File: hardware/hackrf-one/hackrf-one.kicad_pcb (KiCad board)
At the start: 4 copper layers, 120 x 75 mm, 435 parts, among them J10 GND_CLIP, J11 Connector_USB_C_Receptacle_US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, J2 RF-SHIELD-FRAME, J3 RF-SHIELD-COVER, J4 MOUNTING_HOLE, J5 MOUNTING_HOLE, J6 MOUNTING_HOLE, J7 MOUNTING_HOLE, J8 MOUNTING_HOLE, J9 MOUNTING_HOLE, P1 1V8, P13 GPO1, P14 XCVR_CLKOUT, P15 INTR, P16 CLKIN, P17 GPO6, P18 OEB, P19 GPO3, P2 CLKOUT, P20 GPIO, P21 REF_IN, P22 I2S, P23 DBGEN, P24 TRST, P25 LPC_ISP, P26 LPC_JTAG, P27 MIXER_SDATA, P28 SD, P29 CPLD_JTAG, P3 GND, P30 BANK2_AUX, P31 MIXER_SCLK, P32 MIXER_ENX, P33 MIXER_RESETX, P34 MIX_BYPASS, P35 !MIX_BYPASS, P36 VAA, P37 SCL, P38 SDA, P39 SSP1_SCK, P4 ANTENNA, P40 SSP1_MOSI, P41 SSP1_MISO, P43 RX, P44 HP, P45 LP, P46 TX_MIX_BP, P47 RX_MIX_BP, P48 TX_AMP, P49 RX_AMP, P5 LEDS, P50 AMP_BYPASS, P51 !TX_AMP_PWR, P52 !RX_AMP_PWR, P53 CS_XCVR, P54 CS_AD, P55 TXENABLE, P56 RXENABLE, P57 XTAL2, P58 GCK1, P59 GCK2, P6 GPO4, P60 SGPIO_CLK, P61 DA0, P62 DA7, P63 DD0, P64 DD9, P65 DA4, P66 DD5, P67 RSSI, P68 SPIFI_CS, P69 VREGMODE, P7 GPO2, P70 EN_1V8, P72 GP_CLKIN, P73 P1_2, P74 P1_1, P75 GP_CLKIN, P76 GP_CLKIN, P77 GP_CLKIN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

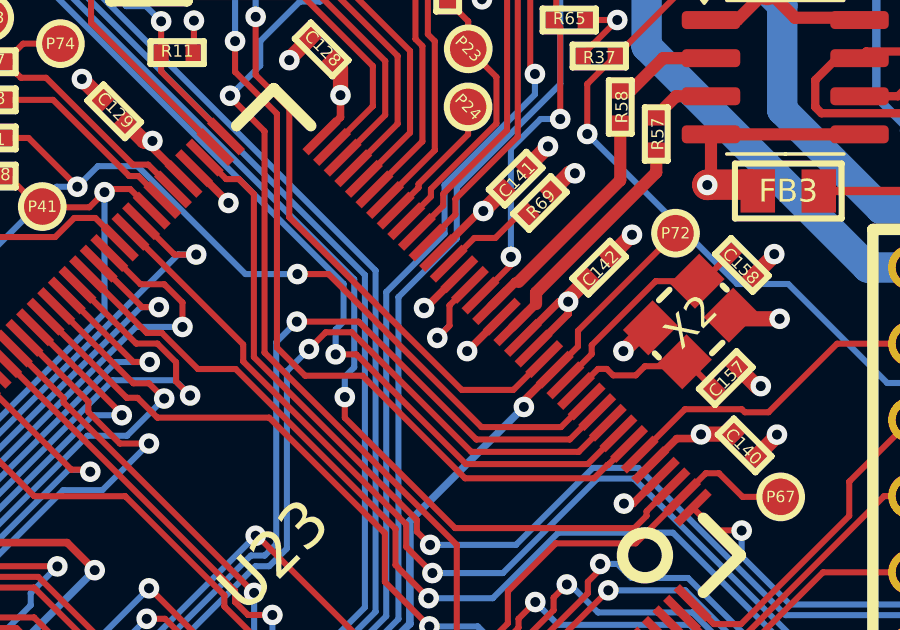
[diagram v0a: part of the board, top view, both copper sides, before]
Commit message: Leave ID pin open, to signal it's a USB device
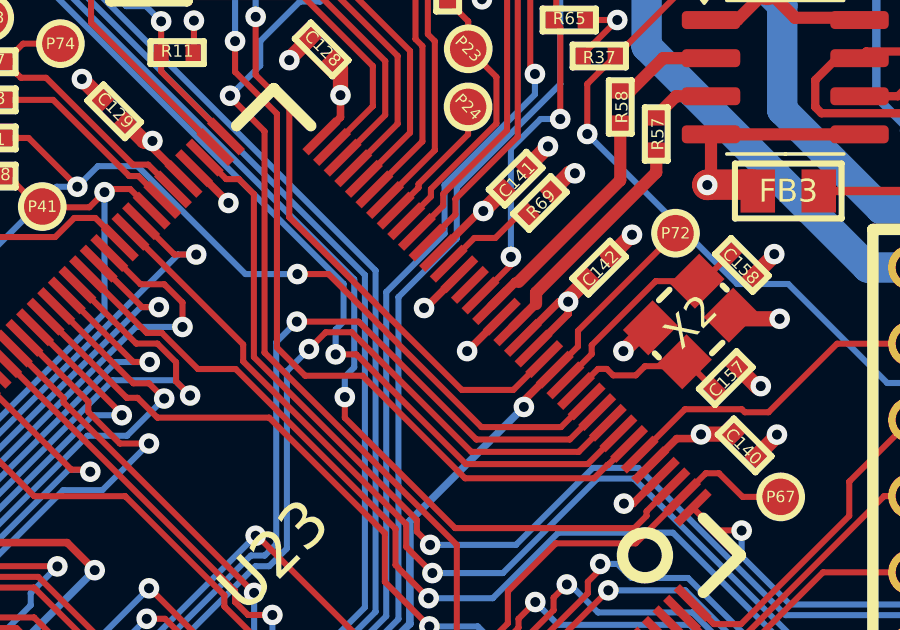
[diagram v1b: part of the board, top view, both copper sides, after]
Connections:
- U23 pad 22: GND -> unconnected-(U23-USB0_ID-Pad22)
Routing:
- net GND: track 599.4 -> 596.7 mm, vias 220 -> 219

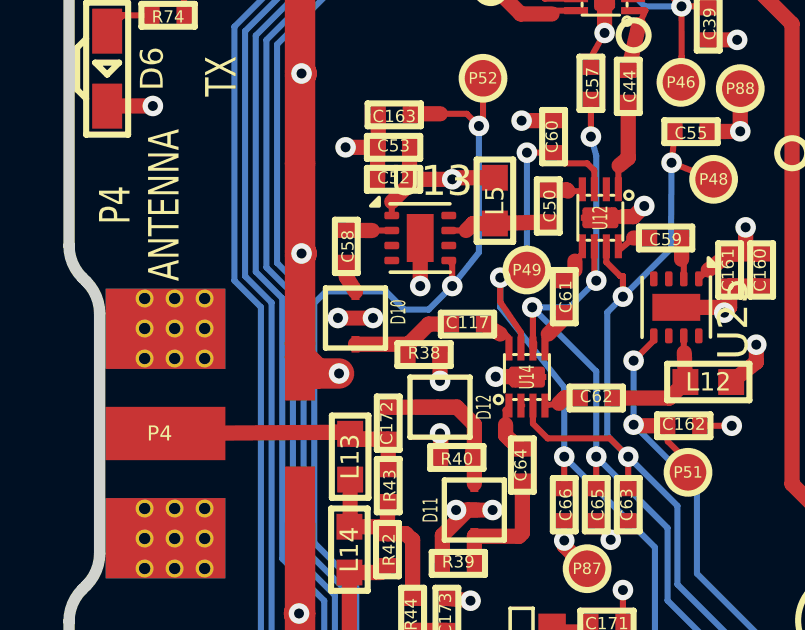
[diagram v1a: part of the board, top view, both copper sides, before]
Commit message: Changed from SMP1330 to CLA4611 to improve performance to 6GHz
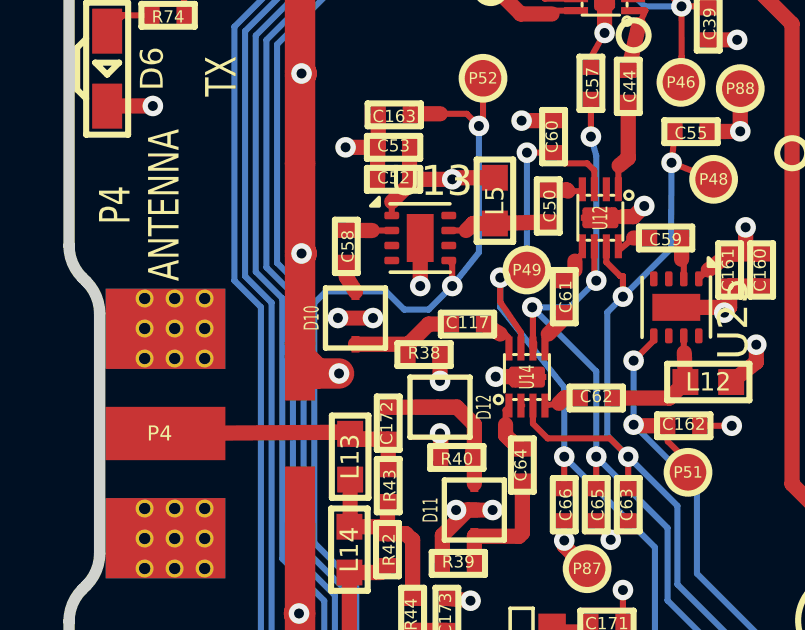
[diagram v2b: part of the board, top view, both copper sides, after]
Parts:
- D10, D11, D12: value SMP1330 -> CLA4611; footprint gsg-modules:SMP1330-085LF -> gsg-modules:SkyworksLimiterDiode
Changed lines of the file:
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@@
 		)
 	)
-	(footprint "gsg-modules:SMP1330-085LF"
+	(footprint "gsg-modules:SkyworksLimiterDiode"
 		(layer "F.Cu")
 		(at 58.3702 139.4058 -90)
 		(property "Reference" "D10"
-			(at -0.20066 -1.43002 90)
+			(at 0 1.4605 90)
 			(layer "F.SilkS")
 			(effects
@@
 			)
 		)
-		(property "Value" "SMP1330"
+		(property "Value" "CLA4611"
 			(at 0 -0.889 90)
 			(layer "F.Fab")
@@
 			)
 		)
-		(property "Footprint" "gsg-modules:SMP1330-085LF"
+		(property "Footprint" "gsg-modules:SkyworksLimiterDiode"
 			(at 0 0 -90)
 			(layer "F.Fab")
@@
 			)
 		)
-		(property "Part Number" "SMP1330-085LF"
-			(at 0 0 -90)
-			(unlocked yes)
-			(layer "F.Fab")
-			(hide yes)
-			(effects
-				(font
-					(size 1 1)
-					(thickness 0.15)
-				)
-			)
-		)
-		(property ki_fp_filters "TO-???* *_Diode_* *SingleDiode* D_*")
+		(property "Part Number" "CLA4611-085LF"
+			(at 0 0 -90)
+			(unlocked yes)
+			(layer "F.Fab")
+			(hide yes)
+			(effects
+				(font
+					(size 1 1)
+					(thickness 0.15)
+				)
+			)
+		)
+		(property ki_fp_filters "PIN_*")
 		(sheetname "frontend")
 		(sheetfile "frontend.kicad_sch")
@@
 		)
 	)
-	(footprint "gsg-modules:SMP1330-085LF"
+	(footprint "gsg-modules:SkyworksLimiterDiode"
 		(layer "F.Cu")
 		(at 62.3326 145.8066 -90)
@@
 			)
 		)
-		(property "Value" "SMP1330"
+		(property "Value" "CLA4611"
 			(at 0 -0.889 90)
 			(layer "F.Fab")
@@
 			)
 		)
-		(property "Footprint" "gsg-modules:SMP1330-085LF"
+		(property "Footprint" "gsg-modules:SkyworksLimiterDiode"
 			(at 0 0 -90)
 			(layer "F.Fab")
@@
 			)
 		)
-		(property "Part Number" "SMP1330-085LF"
-			(at 0 0 -90)
-			(unlocked yes)
-			(layer "F.Fab")
-			(hide yes)
-			(effects
-				(font
-					(size 1 1)
-					(thickness 0.15)
-				)
-			)
-		)
-		(property ki_fp_filters "TO-???* *_Diode_* *SingleDiode* D_*")
+		(property "Part Number" "CLA4611-085LF"
+			(at 0 0 -90)
+			(unlocked yes)
+			(layer "F.Fab")
+			(hide yes)
+			(effects
+				(font
+					(size 1 1)
+					(thickness 0.15)
+				)
+			)
+		)
+		(property ki_fp_filters "PIN_*")
 		(sheetname "frontend")
 		(sheetfile "frontend.kicad_sch")
@@
 		)
 	)
-	(footprint "gsg-modules:SMP1330-085LF"
+	(footprint "gsg-modules:SkyworksLimiterDiode"
 		(layer "F.Cu")
 		(at 61.1896 142.3776 90)
 		(property "Reference" "D12"
-			(at 0 1.4605 90)
+			(at 0 1.4605 -90)
 			(layer "F.SilkS")
 			(effects
@@
 			)
 		)
-		(property "Value" "SMP1330"
-			(at 0 -0.889 90)
+		(property "Value" "CLA4611"
+			(at 0 -0.889 -90)
 			(layer "F.Fab")
 			(effects
@@
 			)
 		)
-		(property "Footprint" "gsg-modules:SMP1330-085LF"
+		(property "Footprint" "gsg-modules:SkyworksLimiterDiode"
 			(at 0 0 90)
 			(layer "F.Fab")
@@
 			)
 		)
-		(property "Part Number" "SMP1330-085LF"
+		(property "Part Number" "CLA4611-085LF"
 			(at 0 0 90)
 			(unlocked yes)
@@
 			)
 		)
-		(property ki_fp_filters "TO-???* *_Diode_* *SingleDiode* D_*")
+		(property ki_fp_filters "PIN_*")
 		(sheetname "frontend")
 		(sheetfile "frontend.kicad_sch")

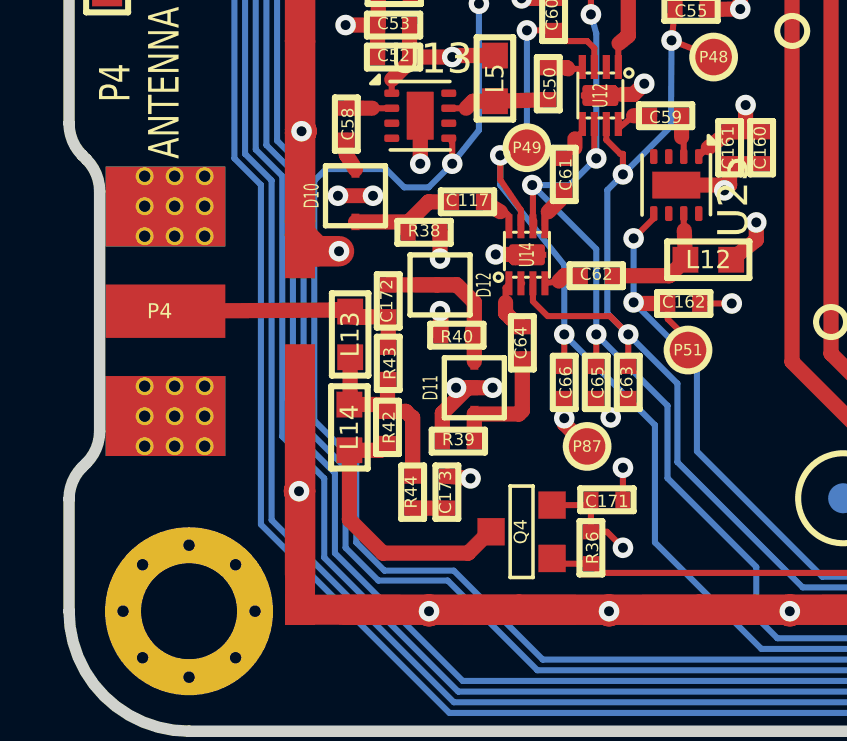
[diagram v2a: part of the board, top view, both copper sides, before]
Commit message: Changed limiter to CLA4611. Added Schottky bias tee diode
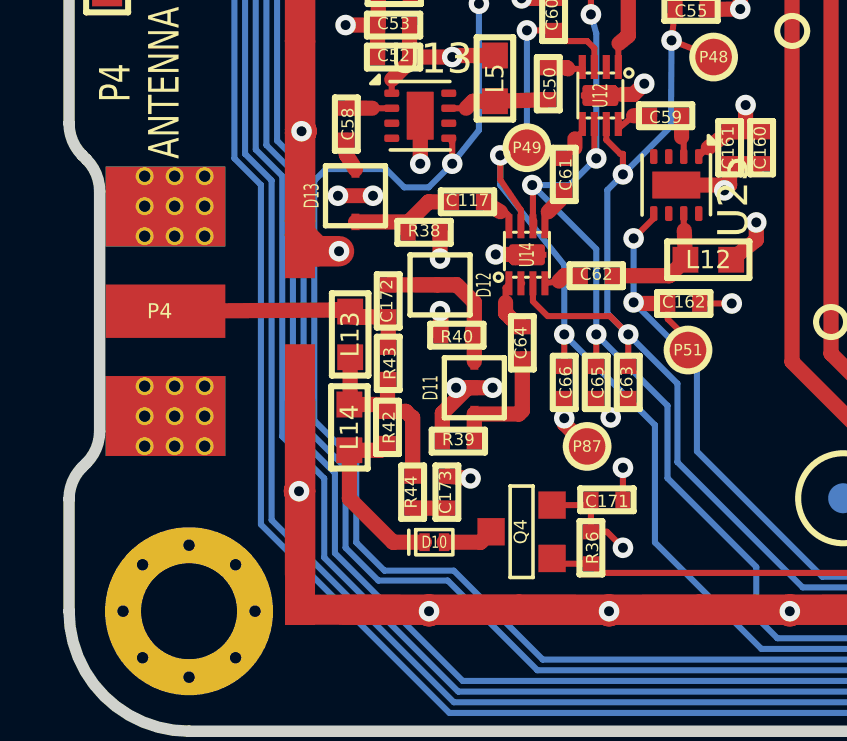
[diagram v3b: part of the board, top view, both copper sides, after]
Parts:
- added D10: D_Schottky, gsg-modules:DSN1006-2, F.Cu at (61.0, 151.0)
- renumbered D10 to D13
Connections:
- L14 pad 1: Net-(L14-Pad1) -> Net-(D10-K)
- Q4 pad D: Net-(L14-Pad1) -> Net-(D10-A)
- R42 pad 1: Net-(L14-Pad1) -> Net-(D10-K)
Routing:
- net Net-(L14-Pad1): track 9.16 -> 0.00 mm
- net Net-(D10-K): track 0.00 -> 6.08 mm
- net Net-(D10-A): track 0.00 -> 1.71 mm
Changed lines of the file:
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@@
 	(net 228 "/frontend/RX_AMP_IN")
 	(net 229 "Net-(C173-Pad2)")
-	(net 230 "Net-(L14-Pad1)")
+	(net 230 "Net-(D13-A2)")
 	(net 231 "Net-(U1-RFC)")
 	(net 232 "Net-(U2-RF1)")
@@
 	(net 269 "Net-(U10-RF1)")
 	(net 270 "Net-(U11-RF2)")
-	(net 271 "Net-(D10-A2)")
+	(net 271 "Net-(D10-K)")
 	(net 272 "Net-(U13-RFIN)")
 	(net 273 "Net-(U25-RFIN)")
@@
 	(net 389 "Net-(FB3-Pad1)")
 	(net 390 "unconnected-(U23-USB0_ID-Pad22)")
+	(net 391 "Net-(D10-A)")
 	(footprint "gsg-modules:LTST-S220"
 		(layer "F.Cu")
@@
 			(size 0.508 0.5588)
 			(layers "F.Cu" "F.Paste" "F.Mask")
-			(net 271 "Net-(D10-A2)")
+			(net 230 "Net-(D13-A2)")
 			(pintype "passive")
 			(die_length -2147.483637)
@@
 			(size 0.9144 0.9144)
 			(layers "F.Cu" "F.Paste" "F.Mask")
-			(net 230 "Net-(L14-Pad1)")
+			(net 391 "Net-(D10-A)")
 			(pinfunction "D")
 			(pintype "passive")
@@
 			(size 0.508 0.5588)
 			(layers "F.Cu" "F.Paste" "F.Mask")
-			(net 230 "Net-(L14-Pad1)")
+			(net 271 "Net-(D10-K)")
 			(pintype "passive")
 			(die_length -2147.483637)
@@
 			(size 0.8636 0.8636)
 			(layers "F.Cu" "F.Paste" "F.Mask")
-			(net 230 "Net-(L14-Pad1)")
+			(net 271 "Net-(D10-K)")
 			(pinfunction "1")
 			(pintype "passive")
@@
 		(layer "F.Cu")
 		(at 58.3702 139.4058 -90)
-		(property "Reference" "D10"
+		(property "Reference" "D13"
 			(at 0 1.4605 90)
 			(layer "F.SilkS")
@@
 			(size 0.55 0.27)
 			(layers "F.Cu" "F.Paste" "F.Mask")
-			(net 271 "Net-(D10-A2)")
+			(net 230 "Net-(D13-A2)")
 			(pinfunction "A2")
 			(pintype "passive")
@@
 		)
 	)
+	(footprint "gsg-modules:DSN1006-2"
+		(layer "F.Cu")
+		(at 60.9976 150.9556)
+		(tags "SOD-993 SOD993")
+		(property "Reference" "D10"
+			(at 0 0 0)
+			(unlocked yes)
+			(layer "F.SilkS")
+			(effects
+				(font
+					(size 0.4064 0.3048)
+					(thickness 0.0762)
+				)
+			)
+		)
+		(property "Value" "D_Schottky"
+			(at 0.025 1.6 0)
+			(unlocked yes)
+			(layer "F.Fab")
+			(effects
+				(font
+					(size 0.5 0.5)
+					(thickness 0.1)
+				)
+			)
+		)
+		(property "Footprint" "gsg-modules:DSN1006-2"
+			(at 0 0 0)
+			(layer "F.Fab")
+			(hide yes)
+			(effects
+				(font
+					(size 1.27 1.27)
+					(thickness 0.15)
+				)
+			)
+		)
+		(property "Datasheet" ""
+			(at 0 0 0)
+			(layer "F.Fab")
+			(hide yes)
+			(effects
+				(font
+					(size 1.27 1.27)
+					(thickness 0.15)
+				)
+			)
+		)
+		(property "Description" "DIODE SCHOTTKY 40V 1A DSN1006-2"
+			(at 0 0 0)
+			(layer "F.Fab")
+			(hide yes)
+			(effects
+				(font
+					(size 1.27 1.27)
+					(thickness 0.15)
+				)
+			)
+		)
+		(property "Manufacturer" "Nexperia"
+			(at 0 0 0)
+			(unlocked yes)
+			(layer "F.Fab")
+			(hide yes)
+			(effects
+				(font
+					(size 1 1)
+					(thickness 0.15)
+				)
+			)
+		)
+		(property "Part Number" "PMEG4010ESBYL"
+			(at 0 0 0)
+			(unlocked yes)
+			(layer "F.Fab")
+			(hide yes)
+			(effects
+				(font
+					(size 1 1)
+					(thickness 0.15)
+				)
+			)
+		)
+		(property ki_fp_filters "TO-???* *_Diode_* *SingleDiode* D_*")
+		(sheetname "frontend")
+		(sheetfile "frontend.kicad_sch")
+		(attr smd)
+		(fp_line
+			(start -0.85 -0.4)
+			(end -0.85 0.4)
+			(stroke
+				(width 0.12)
+				(type solid)
+			)
+			(layer "F.SilkS")
+		)
+		(fp_rect
+			(start -0.62 -0.42)
+			(end 0.62 0.42)
+			(stroke
+				(width 0.12)
+				(type solid)
+			)
+			(fill none)
+			(layer "F.SilkS")
+		)
+		(fp_rect
+			(start -0.65 -0.45)
+			(end 0.65 0.45)
+			(stroke
+				(width 0.05)
+				(type solid)
+			)
+			(fill none)
+			(layer "F.CrtYd")
+		)
+		(fp_line
+			(start -0.2 -0.15)
+			(end -0.2 0.15)
+			(stroke
+				(width 0.1)
+				(type solid)
+			)
+			(layer "F.Fab")
+		)
+		(fp_line
+			(start -0.1 0)
+			(end 0.15 -0.15)
+			(stroke
+				(width 0.1)
+				(type solid)
+			)
+			(layer "F.Fab")
+		)
+		(fp_line
+			(start 0.15 -0.15)
+			(end 0.15 0.15)
+			(stroke
+				(width 0.1)
+				(type solid)
+			)
+			(layer "F.Fab")
+		)
+		(fp_line
+			(start 0.15 0.15)
+			(end -0.1 0)
+			(stroke
+				(width 0.1)
+				(type solid)
+			)
+			(layer "F.Fab")
+		)
+		(fp_rect
+			(start -0.5 -0.3)
+			(end 0.5 0.3)
+			(stroke
+				(width 0.1)
+				(type solid)
+			)
+			(fill none)
+			(layer "F.Fab")
+		)
+		(fp_text user "${REFERENCE}"
+			(at 0.025 0.9 0)
+			(unlocked yes)
+			(layer "F.Fab")
+			(effects
+				(font
+					(size 0.5 0.5)
+					(thickness 0.1)
+				)
+			)
+		)
+		(pad "1" smd rect
+			(at -0.325 0)
+			(size 0.35 0.6)
+			(layers "F.Cu" "F.Paste" "F.Mask")
+			(net 271 "Net-(D10-K)")
+			(pinfunction "K")
+			(pintype "passive")
+		)
+		(pad "2" smd rect
+			(at 0.325 0)
+			(size 0.35 0.6)
+			(layers "F.Cu" "F.Paste" "F.Mask")
+			(net 391 "Net-(D10-A)")
+			(pinfunction "A")
+			(pintype "passive")
+		)
+	)
 	(footprint "hackrf:GSG-0402"
 		(layer "F.Cu")
@@
 	)
 	(segment
-		(start 58.167 147.8894)
-		(end 59.2084 147.8894)
-		(width 0.508)
-		(layer "F.Cu")
-		(net 230)
-	)
-	(segment
-		(start 59.2846 151.3184)
-		(end 62.1294 151.3184)
-		(width 0.508)
-		(layer "F.Cu")
-		(net 230)
-	)
-	(segment
-		(start 59.2084 147.8894)
-		(end 59.437 147.6608)
-		(width 0.508)
-		(layer "F.Cu")
-		(net 230)
-	)
-	(segment
-		(start 58.167 150.2008)
-		(end 59.2846 151.3184)
-		(width 0.508)
-		(layer "F.Cu")
-		(net 230)
-	)
-	(segment
-		(start 62.1294 151.3184)
-		(end 62.8406 150.6072)
-		(width 0.508)
-		(layer "F.Cu")
-		(net 230)
-	)
-	(segment
-		(start 58.167 147.8894)
-		(end 58.167 150.2008)
+		(start 58.0654 138.0342)
+		(end 58.0654 137.5516)
 		(width 0.508)
 		(layer "F.Cu")
@@
 	)
 	(segment
-		(start 62.8406 150.6072)
-		(end 62.8914 150.6072)
+		(start 58.3702 138.5308)
+		(end 58.0654 138.0342)
 		(width 0.508)
 		(layer "F.Cu")
@@
 	)
 	(segment
-		(start 58.0654 138.0342)
-		(end 58.0654 137.5516)
+		(start 58.167 147.8894)
+		(end 59.2084 147.8894)
 		(width 0.508)
 		(layer "F.Cu")
@@
 	)
 	(segment
-		(start 58.3702 138.5308)
-		(end 58.0654 138.0342)
+		(start 58.167 149.5)
+		(end 59.6226 150.9556)
+		(width 0.508)
+		(layer "F.Cu")
+		(net 271)
+	)
+	(segment
+		(start 58.167 147.8894)
+		(end 58.167 149.5)
+		(width 0.508)
+		(layer "F.Cu")
+		(net 271)
+	)
+	(segment
+		(start 59.2084 147.8894)
+		(end 59.437 147.6608)
+		(width 0.508)
+		(layer "F.Cu")
+		(net 271)
+	)
+	(segment
+		(start 59.6226 150.9556)
+		(end 60.6726 150.9556)
 		(width 0.508)
 		(layer "F.Cu")
@@
 		(net 389)
 	)
+	(segment
+		(start 61.3226 150.9556)
+		(end 62.543 150.9556)
+		(width 0.508)
+		(layer "F.Cu")
+		(net 391)
+	)
+	(segment
+		(start 62.543 150.9556)
+		(end 62.8914 150.6072)
+		(width 0.508)
+		(layer "F.Cu")
+		(net 391)
+	)
 	(zone
